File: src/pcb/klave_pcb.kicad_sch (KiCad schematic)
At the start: 0 parts

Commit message: Update schmatic
- matrix
- pico
- reset button
- TRRS connector
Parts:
- added A1: RaspberryPi_Pico, Module_RaspberryPi_Pico:RaspberryPi_Pico_Common, symbol MCU_Module_RaspberryPi_Pico:RaspberryPi_Pico
- added D1: 0:0, symbol Device:D_Small
- added D10: 1:3, symbol Device:D_Small
- added D11: 1:4, symbol Device:D_Small
- added D12: 1:5, symbol Device:D_Small
- added D13: 2:0, symbol Device:D_Small
- added D14: 2:1, symbol Device:D_Small
- added D15: 2:2, symbol Device:D_Small
- added D16: 2:3, symbol Device:D_Small
- added D17: 2:4, symbol Device:D_Small
- added D18: 2:5, symbol Device:D_Small
- added D19: 3:4, symbol Device:D_Small
- added D2: 0:1, symbol Device:D_Small
- added D20: 3:5, symbol Device:D_Small
- added D21: 4:1, symbol Device:D_Small
- added D22: 4:2, symbol Device:D_Small
- added D23: 4:3, symbol Device:D_Small
- added D24: 4:4, symbol Device:D_Small
- added D25: 4:5, symbol Device:D_Small
- added D3: 0:2, symbol Device:D_Small
- added D4: 0:3, symbol Device:D_Small
- added D5: 0:4, symbol Device:D_Small
- added D6: 0:5, symbol Device:D_Small
- added D7: 1:0, symbol Device:D_Small
- added D8: 1:1, symbol Device:D_Small
- added D9: 1:2, symbol Device:D_Small
- added J1: AudioJack4, symbol Connector_Audio:AudioJack4
- added SW1: 0:0, symbol Switch:SW_Push
- added SW10: 1:3, symbol Switch:SW_Push
- added SW11: 1:4, symbol Switch:SW_Push
- added SW12: 1:5, symbol Switch:SW_Push
- added SW13: 2:0, symbol Switch:SW_Push
- added SW14: 2:1, symbol Switch:SW_Push
- added SW15: 2:2, symbol Switch:SW_Push
- added SW16: 2:3, symbol Switch:SW_Push
- added SW17: 2:4, symbol Switch:SW_Push
- added SW18: 2:5, symbol Switch:SW_Push
- added SW19: 3:4, symbol Switch:SW_Push
- added SW2: 0:1, symbol Switch:SW_Push
- added SW20: 3:5, symbol Switch:SW_Push
- added SW21: 4:1, symbol Switch:SW_Push
- added SW22: 4:2, symbol Switch:SW_Push
- added SW23: 4:3, symbol Switch:SW_Push
- added SW24: 4:4, symbol Switch:SW_Push
- added SW25: 4:5, symbol Switch:SW_Push
- added SW26: SW_Push, symbol Switch:SW_Push
- added SW3: 0:2, symbol Switch:SW_Push
- added SW4: 0:3, symbol Switch:SW_Push
- added SW5: 0:4, symbol Switch:SW_Push
- added SW6: 0:5, symbol Switch:SW_Push
- added SW7: 1:0, symbol Switch:SW_Push
- added SW8: 1:1, symbol Switch:SW_Push
- added SW9: 1:2, symbol Switch:SW_Push
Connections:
- new net: D22.2 (A), SW22.2
- new net: D5.2 (A), SW5.2
- new net: D10.2 (A), SW10.2
- new net: D13.2 (A), SW13.2
- new net: D2.2 (A), SW2.2
- new net: D25.2 (A), SW25.2
- new net: D23.2 (A), SW23.2
- new net: D14.2 (A), SW14.2
- new net: D4.2 (A), SW4.2
- new net: D12.2 (A), SW12.2
- new net: D21.2 (A), SW21.2
- new net: D19.2 (A), SW19.2
- new net: D16.2 (A), SW16.2
- new net: D8.2 (A), SW8.2
- new net: D11.2 (A), SW11.2
- new net: D1.2 (A), SW1.2
- new net: D15.2 (A), SW15.2
- new net: D18.2 (A), SW18.2
- new net: D6.2 (A), SW6.2
- new net: D20.2 (A), SW20.2
- new net: D24.2 (A), SW24.2
- new net: D3.2 (A), SW3.2
- new net: D9.2 (A), SW9.2
- new net: D17.2 (A), SW17.2
- new net: D7.2 (A), SW7.2
- new net COL_{L0}: A1.14 (GPIO10), SW1.1, SW13.1, SW7.1
- new net COL_{L1}: A1.15 (GPIO11), SW14.1, SW2.1, SW21.1, SW8.1
- new net COL_{L2}: A1.16 (GPIO12), SW15.1, SW22.1, SW3.1, SW9.1
- new net COL_{L3}: A1.17 (GPIO13), SW10.1, SW16.1, SW23.1, SW4.1
- new net COL_{L4}: A1.19 (GPIO14), SW11.1, SW17.1, SW19.1, SW24.1, SW5.1
- new net COL_{L5}: A1.20 (GPIO15), SW12.1, SW18.1, SW20.1, SW25.1, SW6.1
- new net GND_{L}: A1.13 (GND), A1.18 (GND), A1.23 (GND), A1.28 (GND), A1.3 (GND), A1.38 (GND), A1.8 (GND), J1.S, SW26.2
- new net RESET_{L}: A1.30 (RUN), SW26.1
- new net ROW_{L0}: A1.26 (GPIO20), D1.1 (K), D2.1 (K), D3.1 (K), D4.1 (K), D5.1 (K), D6.1 (K)
- new net ROW_{L1}: A1.25 (GPIO19), D10.1 (K), D11.1 (K), D12.1 (K), D7.1 (K), D8.1 (K), D9.1 (K)
- new net ROW_{L2}: A1.24 (GPIO18), D13.1 (K), D14.1 (K), D15.1 (K), D16.1 (K), D17.1 (K), D18.1 (K)
- new net ROW_{L3}: A1.22 (GPIO17), D19.1 (K), D20.1 (K)
- new net ROW_{L4}: A1.21 (GPIO16), D21.1 (K), D22.1 (K), D23.1 (K), D24.1 (K), D25.1 (K)
- new net RX_{L}: A1.2 (GPIO1), J1.R1
- new net TX_{L}: A1.1 (GPIO0), J1.R2
- new net VCC_{L}: A1.39 (VSYS), J1.T
- no-connect marks 0 -> 18

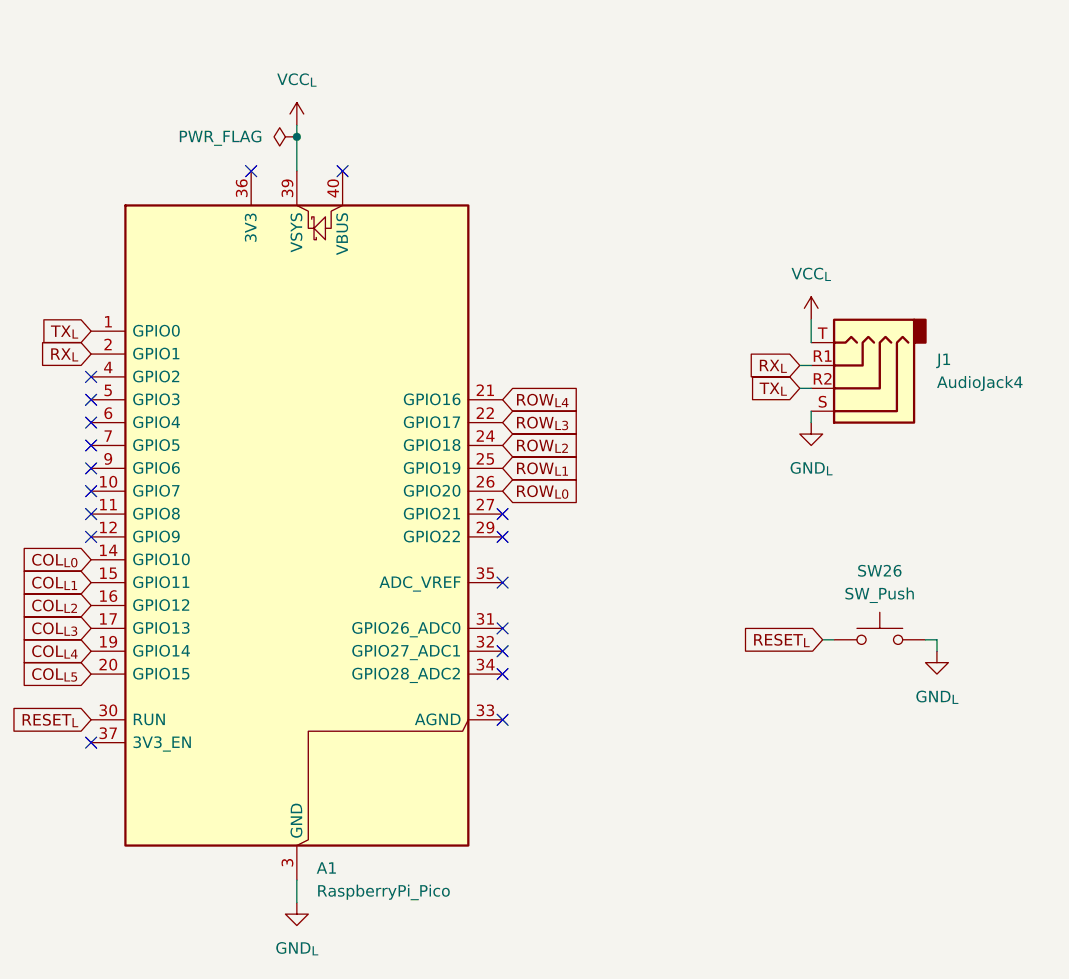
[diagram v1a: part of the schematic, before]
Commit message: Pull up a pin for handedness
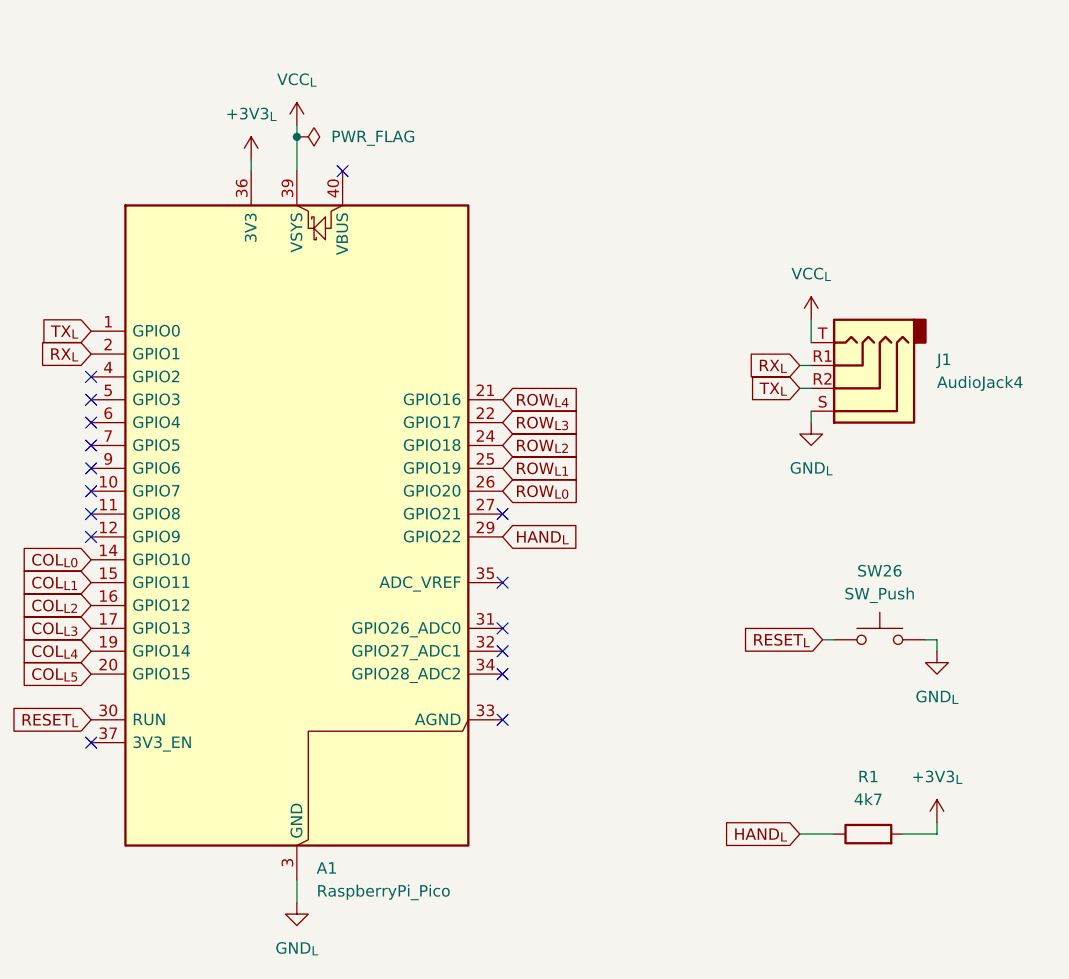
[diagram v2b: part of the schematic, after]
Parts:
- added R1: 4k7, symbol Device:R
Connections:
- net HAND_{L}: now reaches A1.29 (GPIO22)
- net HAND_{L}: now also R1.1
- net +3V3_{L}: now reaches A1.36 (3V3)
- net +3V3_{L}: now also R1.2
- no-connect marks 18 -> 16

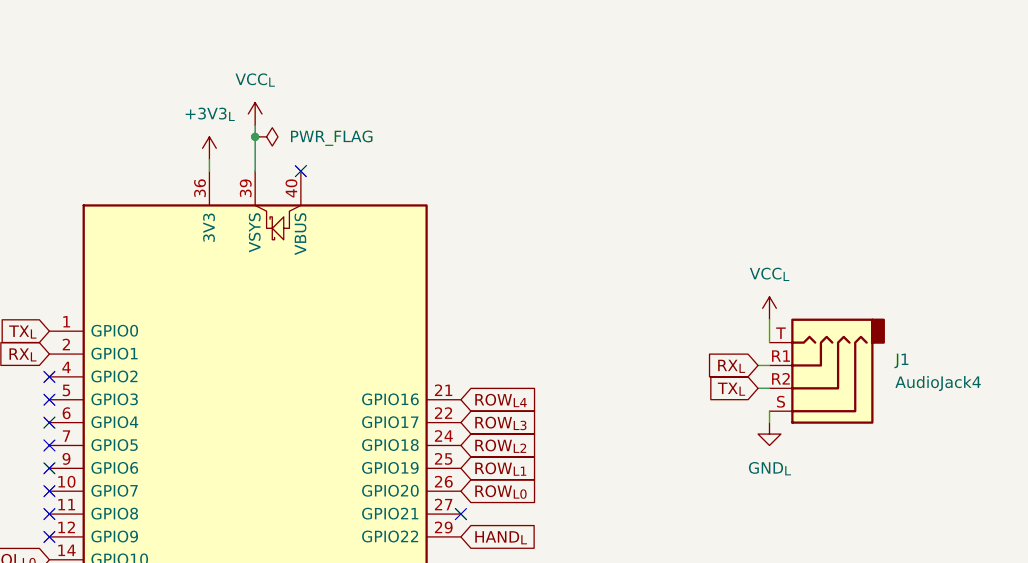
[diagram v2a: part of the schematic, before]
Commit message: Swap TX and RX on TRRS
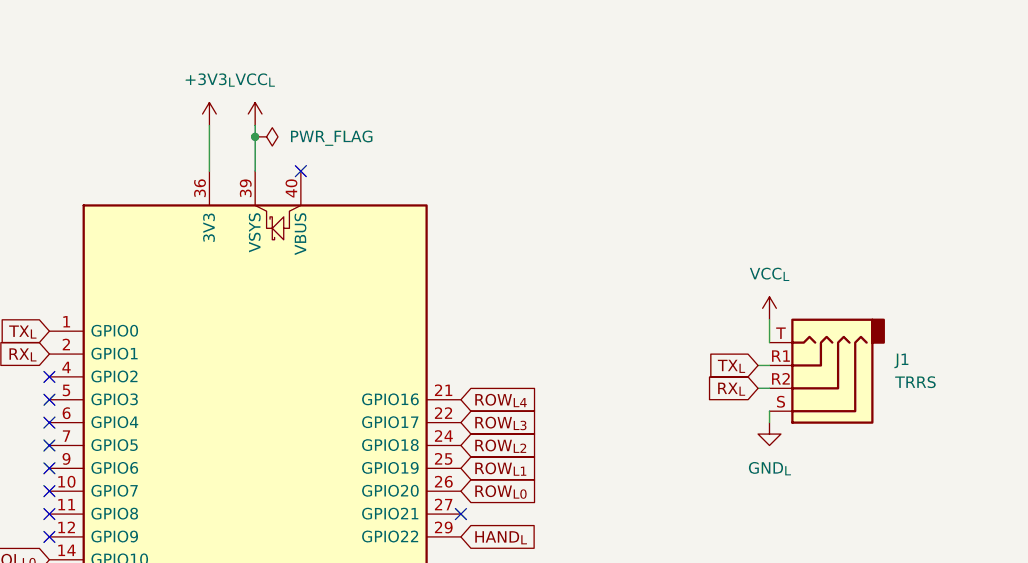
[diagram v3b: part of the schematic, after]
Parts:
- J1: value AudioJack4 -> TRRS
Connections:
- net RX_{L}: now also J1.R2; no longer J1.R1
- net TX_{L}: now also J1.R1; no longer J1.R2
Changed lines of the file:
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@@
 	(wire
 		(pts
-			(xy 179.07 25.4) (xy 179.07 26.67)
+			(xy 179.07 21.59) (xy 179.07 26.67)
 		)
 		(stroke
@@
 	(global_label "RX_{L}"
 		(shape input)
-		(at 240.03 48.26 180)
+		(at 240.03 50.8 180)
 		(fields_autoplaced yes)
 		(effects
@@
 		)
 		(property "Intersheetrefs" "${INTERSHEET_REFS}"
-			(at 233.692 48.26 0)
+			(at 233.692 50.8 0)
 			(effects
 				(font
@@
 	(global_label "TX_{L}"
 		(shape input)
-		(at 240.03 50.8 180)
+		(at 240.03 48.26 180)
 		(fields_autoplaced yes)
 		(effects
@@
 		)
 		(property "Intersheetrefs" "${INTERSHEET_REFS}"
-			(at 233.9944 50.8 0)
+			(at 233.9944 48.26 0)
 			(effects
 				(font
@@
 			)
 		)
-		(property "Value" "AudioJack4"
+		(property "Value" "TRRS"
 			(at 255.27 50.1649 0)
 			(effects
@@
 	(symbol
 		(lib_id "power:+3V3")
-		(at 179.07 25.4 0)
+		(at 179.07 21.59 0)
 		(unit 1)
 		(exclude_from_sim no)
@@
 		(fields_autoplaced yes)
 		(property "Reference" "#PWR07"
-			(at 179.07 29.21 0)
+			(at 179.07 25.4 0)
 			(effects
 				(font
@@
 		)
 		(property "Value" "+3V3_{L}"
-			(at 179.07 20.32 0)
+			(at 179.07 16.51 0)
 			(effects
 				(font
@@
 		)
 		(property "Footprint" ""
-			(at 179.07 25.4 0)
+			(at 179.07 21.59 0)
 			(effects
 				(font
@@
 		)
 		(property "Datasheet" ""
-			(at 179.07 25.4 0)
+			(at 179.07 21.59 0)
 			(effects
 				(font
@@
 		)
 		(property "Description" "Power symbol creates a global label with name \"+3V3\""
-			(at 179.07 25.4 0)
+			(at 179.07 21.59 0)
 			(effects
 				(font
